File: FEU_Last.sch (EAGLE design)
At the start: 67 parts, among them IC1 LM358N, IC3 FT232RL, Q1 8M, Q2 32748, X2 MINI-USB-32005-201

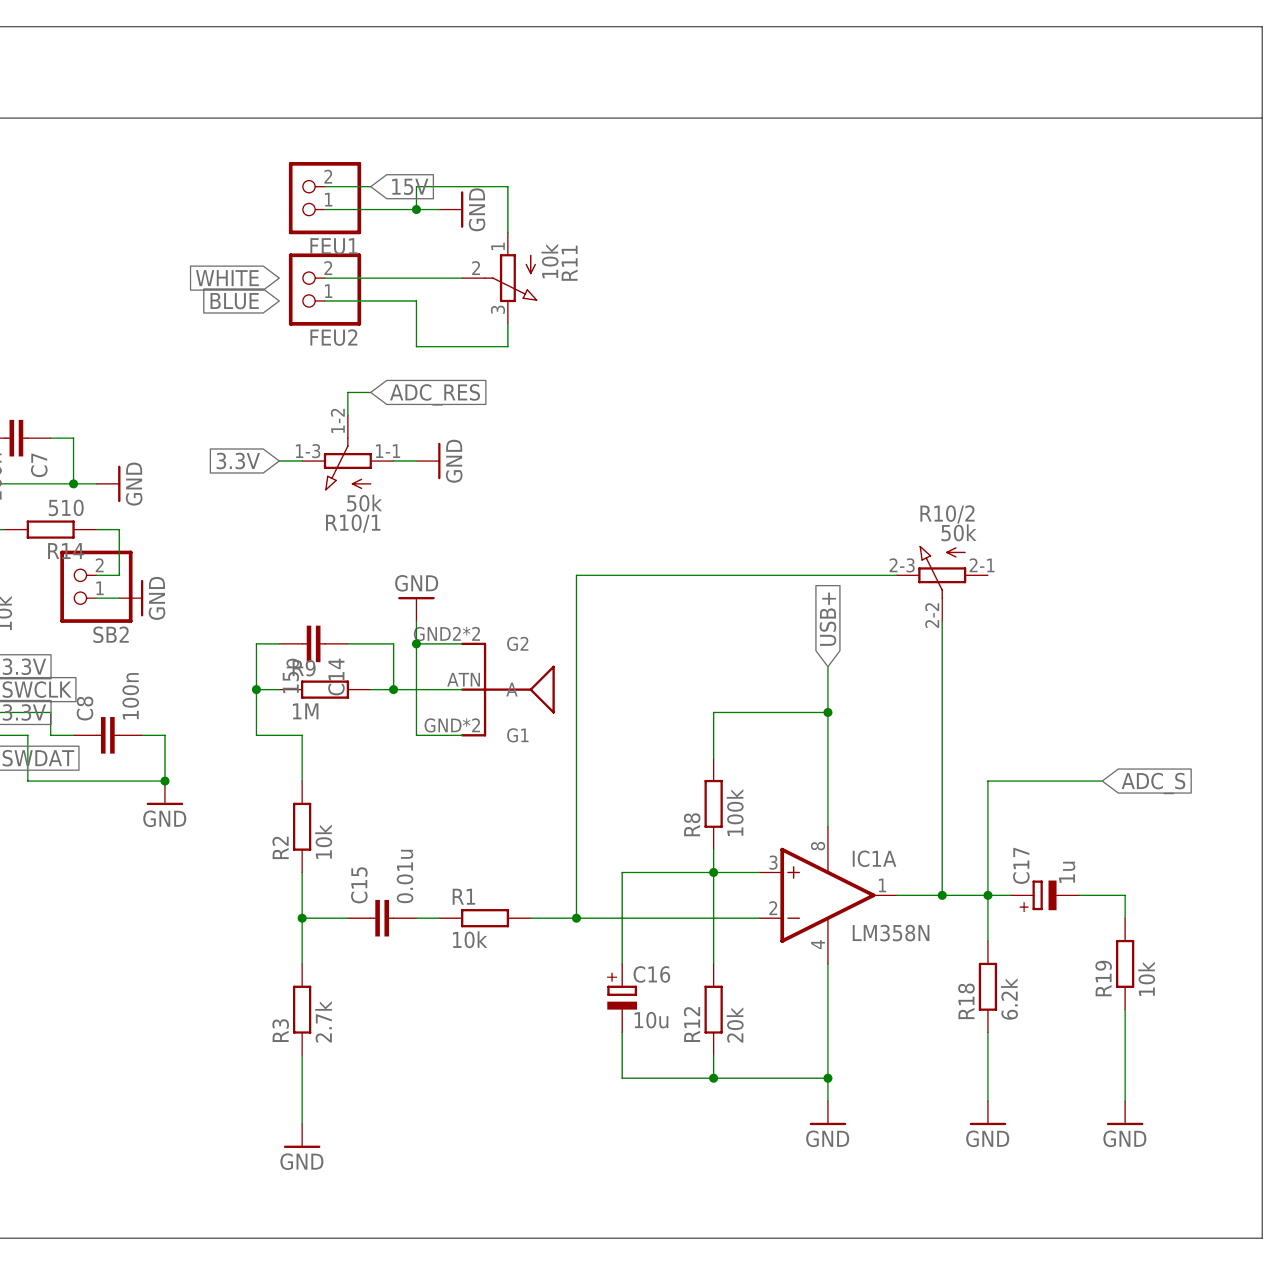
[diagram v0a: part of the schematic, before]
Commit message: Add current-to voltage converter
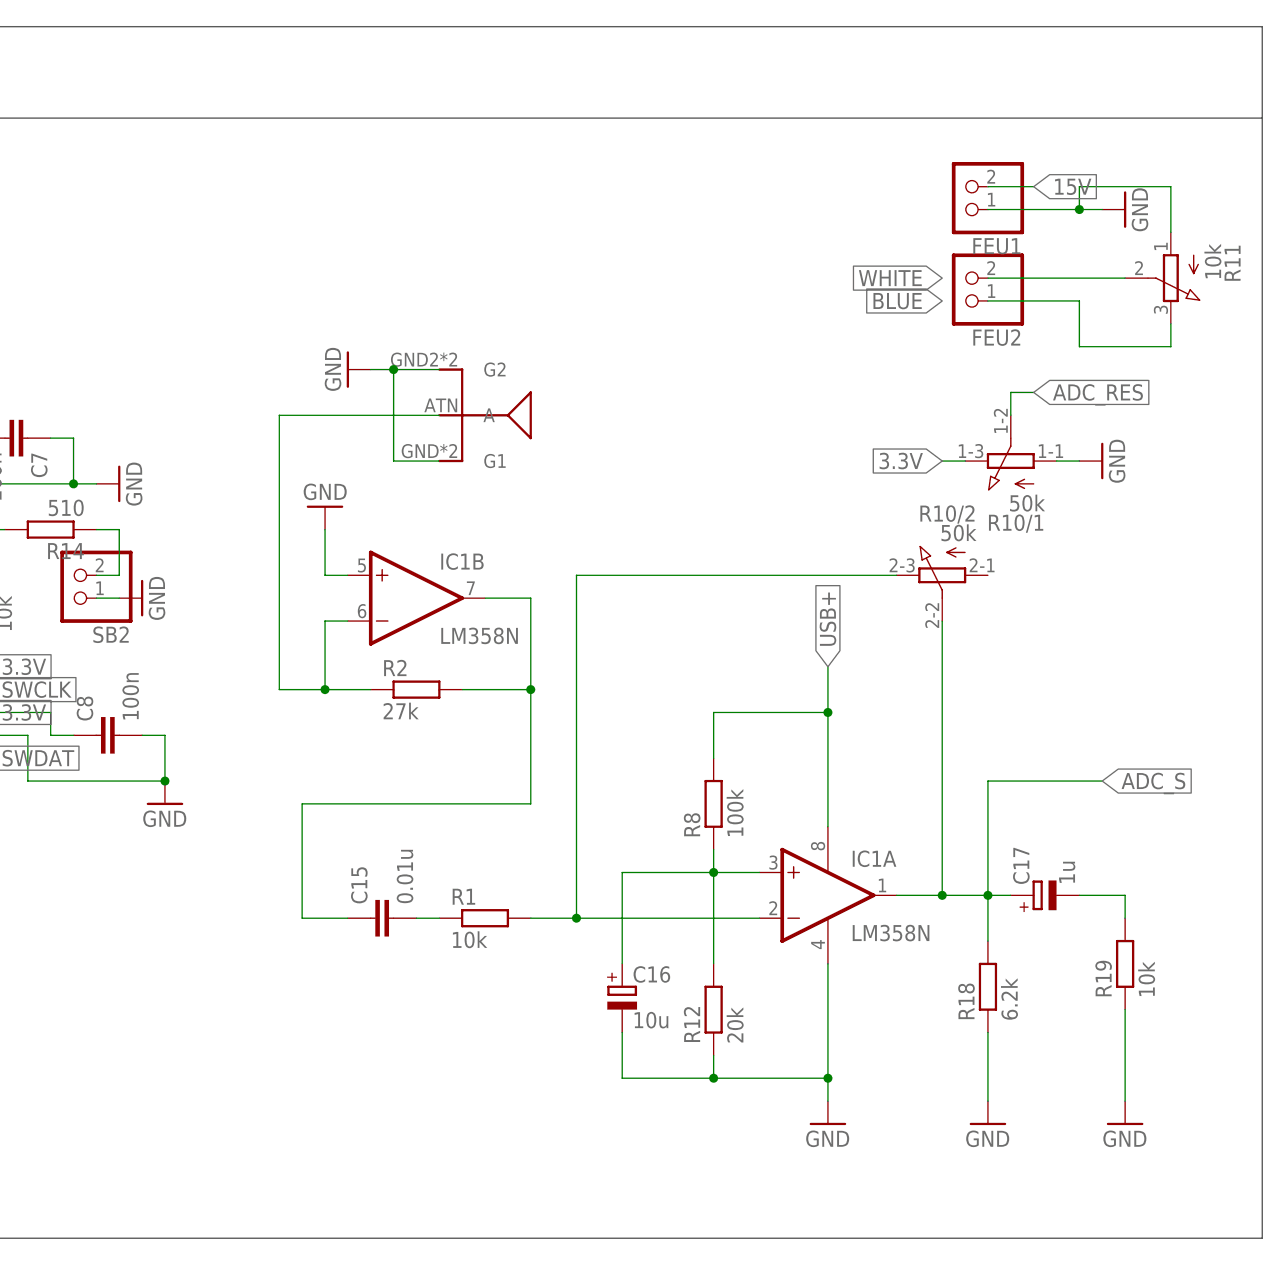
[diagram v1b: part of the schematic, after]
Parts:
- removed C14: 15p, resistor:C-EUC0805
- removed R3: 2.7k, resistor:R-EU_R0805
- removed R9: 1M, resistor:R-EU_R0805
- R2: value 10k -> 27k
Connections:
- removed net N$8: C14.2, R2.2, R9.1
- net GND: now also IC1B.+IN; no longer R3.1
- net N$6: now also IC1B.-IN, U$2.A; no longer C15.1, R3.2
- net N$7: now also C15.1, IC1B.OUT, R2.2; no longer C14.1, R9.2, U$2.A
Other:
- moved on the sheet: FEU1, FEU2, R10/1, R11, R2
